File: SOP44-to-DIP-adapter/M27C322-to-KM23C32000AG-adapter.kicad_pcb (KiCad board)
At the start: 2 copper layers, 14.9 x 28.7 mm, 2 parts, among them J1 PinSocket_2x22_P1.27mm_Vertic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, U1 KM23C32000AG-adaptor

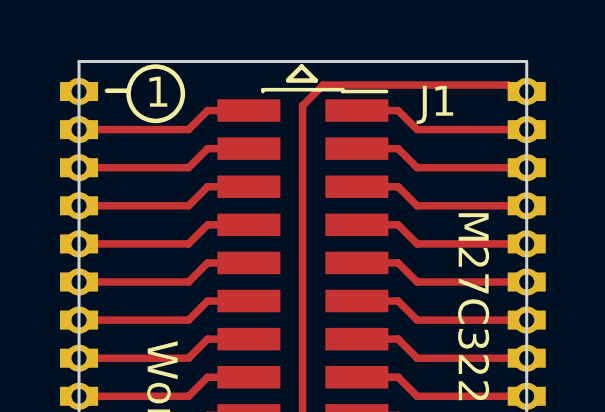
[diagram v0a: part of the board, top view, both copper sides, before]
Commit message: rename projects, update design
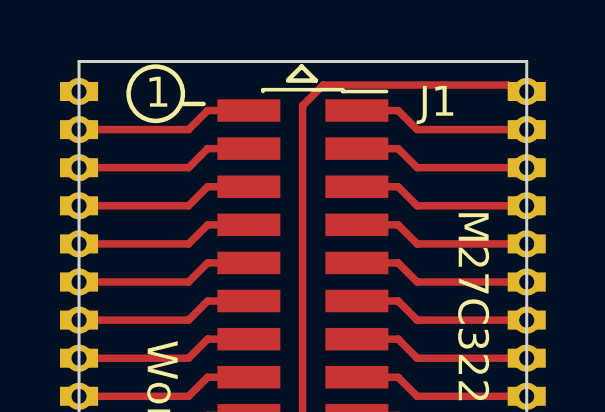
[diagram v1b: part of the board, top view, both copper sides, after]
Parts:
- J1: value PinSocket_2x22_P1.27mm_Vertical -> PinSocket_2x21_P1.27mm_Vertical
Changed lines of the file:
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@@
       (effects (font (size 1 1) (thickness 0.15)))
     )
-    (fp_text value "PinSocket_2x22_P1.27mm_Vertical" (at 0 14.835) (layer "F.Fab")
+    (fp_text value "PinSocket_2x21_P1.27mm_Vertical" (at 0 14.835) (layer "F.Fab")
       (effects (font (size 1 1) (thickness 0.15)))
     )
@@
   (gr_line (start 148.78 67.5) (end 149.25 67.97) (layer "F.SilkS") (width 0.15))
   (gr_circle (center 143.914904 68.41) (end 144.554904 69.05) (layer "F.SilkS") (width 0.15) (fill none))
-  (gr_line (start 143.01 68.31) (end 142.29 68.31) (layer "F.SilkS") (width 0.15))
+  (gr_line (start 144.79 68.75) (end 145.51 68.75) (layer "F.SilkS") (width 0.15))
   (gr_line (start 148.33 67.95) (end 148.78 67.5) (layer "F.SilkS") (width 0.15))
   (gr_rect (start 141.359 67.335) (end 156.2815 96.005) (layer "Edge.Cuts") (width 0.1) (fill none))
